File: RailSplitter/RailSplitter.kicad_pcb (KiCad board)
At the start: 2 copper layers, 75 x 45 mm, 24 parts, among them J1 Screw_Terminal_01x02, J2 Screw_Terminal_01x03, Q1 DMP6180SK3, Q2 NJVMJB42CT4G, Q3 NJVMJB41CT4G, U1 OPA990

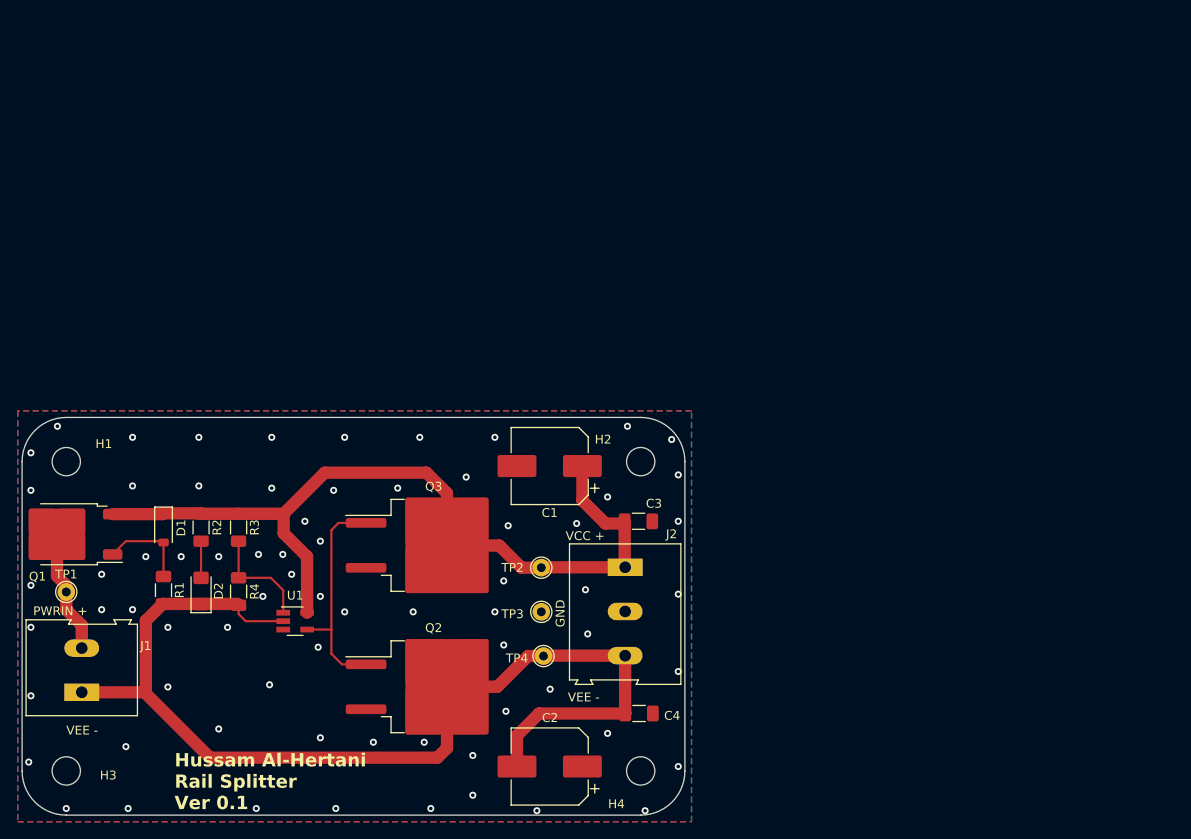
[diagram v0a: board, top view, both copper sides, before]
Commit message: Sat: Apr 27 Added Dual H-Bridge Daughterboard and fixed railsplitter
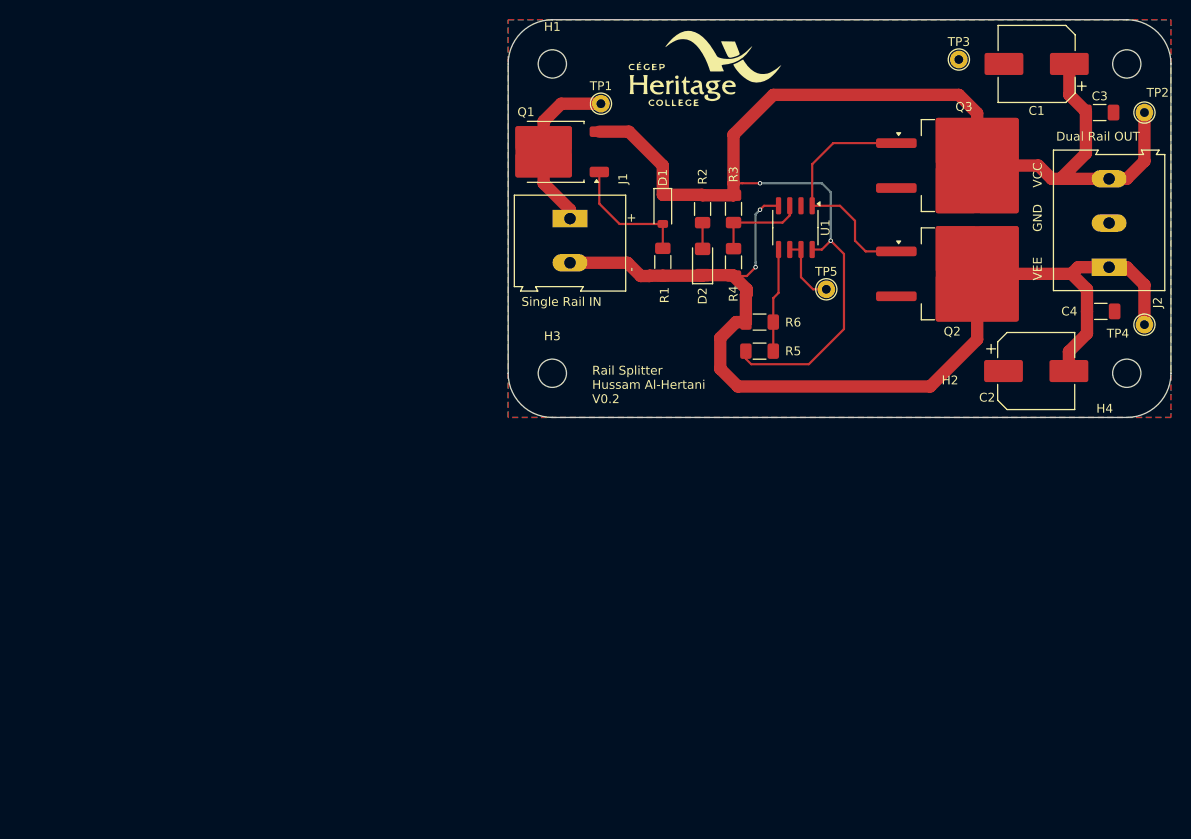
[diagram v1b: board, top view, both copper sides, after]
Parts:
- added G***: LOGO, logos:heritage-logo-small, F.Cu at (172.0, 55.5)
- added R5: 10k, Resistor_SMD:R_1206_3216Metric_Pad1.30x1.75mm_HandSolder, F.Cu at (178.4, 87.5)
- added R6: 10k, Resistor_SMD:R_1206_3216Metric_Pad1.30x1.75mm_HandSolder, F.Cu at (178.4, 84.2)
- added TP5: TestPoint, TestPoint:TestPoint_THTPad_D2.0mm_Drill1.0mm, F.Cu at (186.0, 80.5)
- U1: value OPA990 -> OPA2990IDR; footprint Package_TO_SOT_SMD:SOT-23-5_HandSoldering -> Package_SO:SOIC-8_3.9x4.9mm_P1.27mm
- moved TP2 85.5 mm to (222.0, 60.5)
- moved TP1 81.9 mm to (160.5, 59.5)
- moved TP3 78.4 mm to (201.0, 54.5)
- moved TP4 77.7 mm to (222.0, 84.5)
- moved J1 77.0 mm to (157.0, 72.5), turned to -90 degrees
- moved Q2 76.0 mm to (201.6, 78.8)
- moved Q3 73.8 mm to (201.6, 66.5)
- moved U1 72.0 mm to (182.5, 73.5), turned to -90 degrees
- moved C1 71.5 mm to (209.8, 55.0)
- moved H1 71.1 mm to (155.0, 55.0)
- moved H2 71.1 mm to (220.0, 55.0)
- moved H3 71.1 mm to (155.0, 90.0)
- moved H4 71.1 mm to (220.0, 90.0)
- moved C2 70.9 mm to (209.8, 89.8), turned to 0 degrees
- moved Q1 70.0 mm to (155.3, 64.9)
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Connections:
- J1 pad 1: VEE -> /PWRIN
- J1 pad 2: /PWRIN -> VEE
- J2 pad 1: VCC -> VEE
- J2 pad 3: VEE -> VCC
- R3 pad 2: Net-(U1-+) -> Net-(U1A-+)
- R4 pad 1: Net-(U1-+) -> Net-(U1A-+)
- U1 pad 1: Net-(U1-+) -> Net-(Q2-B)
- U1 pad 2: VEE -> GND
- U1 pad 3: GND -> Net-(U1A-+)
- U1 pad 4: Net-(Q2-B) -> VEE
- U1 pad 5: VCC -> Net-(U1B-+)
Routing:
- net VCC: track 95.2 -> 147.9 mm, vias 0 -> 2
- net Net-(U1-+): track 12.3 -> 0.00 mm
- net Net-(U1B-+): track 0.00 -> 11.7 mm
- net Net-(U1A-+): track 0.00 -> 10.7 mm
- net Net-(U1B--): track 0.00 -> 7.84 mm
- net /PWRIN: track 14.0 -> 19.6 mm
- net Net-(D1-A): track 10.3 -> 14.5 mm
- net Net-(Q2-B): track 25.4 -> 28.2 mm
- net VEE: track 122.6 -> 120.8 mm, vias 0 -> 2
- net Net-(D2-A): track 4.15 -> 2.96 mm
- net GND: vias 71 -> 0
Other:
- board text added: "+"
- board text added: "-"
- board text added: "Dual Rail OUT"
- board text added: "Rail Splitter Hussam Al-Hertani V0.2"
- board text added: "Single Rail IN"
- board text added: "VCC"
- board text added: "VEE"
- board text removed: "Hussam Al-Hertani Rail Splitter Ver 0.1"
- board text removed: "PWRIN +"
- board text removed: "VCC +"
- board text removed: "VEE -"

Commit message: Added16 Channel Servo controller Design
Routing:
- net GND: vias 0 -> 90

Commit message: created _latest gerber sets and added digikey boms. Also did some project cleanup WedMay82024
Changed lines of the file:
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@@
 			(size 1.425 1.75)
 			(layers "F.Cu" "F.Paste" "F.Mask")
-			(roundrect_rratio 0.175439)
+			(roundrect_rratio 0.1754392982)
 			(net 3 "VEE")
 			(pinfunction "K")
@@
 			(size 1.425 1.75)
 			(layers "F.Cu" "F.Paste" "F.Mask")
-			(roundrect_rratio 0.175439)
+			(roundrect_rratio 0.1754392982)
 			(net 5 "Net-(D2-A)")
 			(pinfunction "A")
@@
 			(size 4.6 1.1)
 			(layers "F.Cu" "F.Paste" "F.Mask")
-			(roundrect_rratio 0.227273)
+			(roundrect_rratio 0.2272727273)
 			(net 7 "Net-(Q2-B)")
 			(pinfunction "B")
@@
 			(size 4.55 5.25)
 			(layers "F.Cu" "F.Paste")
-			(roundrect_rratio 0.054945)
+			(roundrect_rratio 0.05494505495)
 			(net 1 "VCC")
 			(pinfunction "C")
@@
 			(size 4.55 5.25)
 			(layers "F.Cu" "F.Paste")
-			(roundrect_rratio 0.054945)
+			(roundrect_rratio 0.05494505495)
 			(net 1 "VCC")
 			(pinfunction "C")
@@
 			(size 9.4 10.8)
 			(layers "F.Cu" "F.Mask")
-			(roundrect_rratio 0.026596)
+			(roundrect_rratio 0.02659595745)
 			(net 1 "VCC")
 			(pinfunction "C")
@@
 			(size 4.55 5.25)
 			(layers "F.Cu" "F.Paste")
-			(roundrect_rratio 0.054945)
+			(roundrect_rratio 0.05494505495)
 			(net 1 "VCC")
 			(pinfunction "C")
@@
 			(size 4.55 5.25)
 			(layers "F.Cu" "F.Paste")
-			(roundrect_rratio 0.054945)
+			(roundrect_rratio 0.05494505495)
 			(net 1 "VCC")
 			(pinfunction "C")
@@
 			(size 4.6 1.1)
 			(layers "F.Cu" "F.Paste" "F.Mask")
-			(roundrect_rratio 0.227273)
+			(roundrect_rratio 0.2272727273)
 			(net 2 "GND")
 			(pinfunction "E")
@@
 			(size 1.3 1.75)
 			(layers "F.Cu" "F.Paste" "F.Mask")
-			(roundrect_rratio 0.192308)
+			(roundrect_rratio 0.1923076923)
 			(net 1 "VCC")
 			(pintype "passive")
@@
 			(size 1.3 1.75)
 			(layers "F.Cu" "F.Paste" "F.Mask")
-			(roundrect_rratio 0.192308)
+			(roundrect_rratio 0.1923076923)
 			(net 5 "Net-(D2-A)")
 			(pintype "passive")
@@
 			(size 1.3 1.75)
 			(layers "F.Cu" "F.Paste" "F.Mask")
-			(roundrect_rratio 0.192308)
+			(roundrect_rratio 0.1923076923)
 			(net 4 "Net-(D1-A)")
 			(pintype "passive")
@@
 			(size 1.3 1.75)
 			(layers "F.Cu" "F.Paste" "F.Mask")
-			(roundrect_rratio 0.192308)
+			(roundrect_rratio 0.1923076923)
 			(net 3 "VEE")
 			(pintype "passive")
@@
 			(size 1.3 1.75)
 			(layers "F.Cu" "F.Paste" "F.Mask")
-			(roundrect_rratio 0.192308)
+			(roundrect_rratio 0.1923076923)
 			(net 1 "VCC")
 			(pintype "passive")
@@
 			(size 1.3 1.75)
 			(layers "F.Cu" "F.Paste" "F.Mask")
-			(roundrect_rratio 0.192308)
+			(roundrect_rratio 0.1923076923)
 			(net 9 "Net-(U1B-+)")
 			(pintype "passive")
@@
 			(size 4.6 1.1)
 			(layers "F.Cu" "F.Paste" "F.Mask")
-			(roundrect_rratio 0.227273)
+			(roundrect_rratio 0.2272727273)
 			(net 7 "Net-(Q2-B)")
 			(pinfunction "B")
@@
 			(size 4.55 5.25)
 			(layers "F.Cu" "F.Paste")
-			(roundrect_rratio 0.054945)
+			(roundrect_rratio 0.05494505495)
 			(net 3 "VEE")
 			(pinfunction "C")
@@
 			(size 4.55 5.25)
 			(layers "F.Cu" "F.Paste")
-			(roundrect_rratio 0.054945)
+			(roundrect_rratio 0.05494505495)
 			(net 3 "VEE")
 			(pinfunction "C")
@@
 			(size 9.4 10.8)
 			(layers "F.Cu" "F.Mask")
-			(roundrect_rratio 0.026596)
+			(roundrect_rratio 0.02659595745)
 			(net 3 "VEE")
 			(pinfunction "C")
@@
 			(size 4.55 5.25)
 			(layers "F.Cu" "F.Paste")
-			(roundrect_rratio 0.054945)
+			(roundrect_rratio 0.05494505495)
 			(net 3 "VEE")
 			(pinfunction "C")
@@
 			(size 4.55 5.25)
 			(layers "F.Cu" "F.Paste")
-			(roundrect_rratio 0.054945)
+			(roundrect_rratio 0.05494505495)
 			(net 3 "VEE")
 			(pinfunction "C")
@@
 			(size 4.6 1.1)
 			(layers "F.Cu" "F.Paste" "F.Mask")
-			(roundrect_rratio 0.227273)
+			(roundrect_rratio 0.2272727273)
 			(net 2 "GND")
 			(pinfunction "E")
@@
 			(size 2.2 1.2)
 			(layers "F.Cu" "F.Paste" "F.Mask")
-			(roundrect_rratio 0.208333)
+			(roundrect_rratio 0.2083333333)
 			(net 4 "Net-(D1-A)")
 			(pinfunction "G")
@@
 			(size 3.05 2.75)
 			(layers "F.Cu" "F.Paste")
-			(roundrect_rratio 0.090909)
+			(roundrect_rratio 0.09090909091)
 			(net 6 "/PWRIN")
 			(pinfunction "D")
@@
 			(size 3.05 2.75)
 			(layers "F.Cu" "F.Paste")
-			(roundrect_rratio 0.090909)
+			(roundrect_rratio 0.09090909091)
 			(net 6 "/PWRIN")
 			(pinfunction "D")
@@
 			(size 6.4 5.8)
 			(layers "F.Cu" "F.Mask")
-			(roundrect_rratio 0.043103)
+			(roundrect_rratio 0.04310293103)
 			(net 6 "/PWRIN")
 			(pinfunction "D")
@@
 			(size 3.05 2.75)
 			(layers "F.Cu" "F.Paste")
-			(roundrect_rratio 0.090909)
+			(roundrect_rratio 0.09090909091)
 			(net 6 "/PWRIN")
 			(pinfunction "D")
@@
 			(size 3.05 2.75)
 			(layers "F.Cu" "F.Paste")
-			(roundrect_rratio 0.090909)
+			(roundrect_rratio 0.09090909091)
 			(net 6 "/PWRIN")
 			(pinfunction "D")
@@
 			(size 2.2 1.2)
 			(layers "F.Cu" "F.Paste" "F.Mask")
-			(roundrect_rratio 0.208333)
+			(roundrect_rratio 0.2083333333)
 			(net 1 "VCC")
 			(pinfunction "S")
@@
 			(size 1.3 1.75)
 			(layers "F.Cu" "F.Paste" "F.Mask")
-			(roundrect_rratio 0.192308)
+			(roundrect_rratio 0.1923076923)
 			(net 9 "Net-(U1B-+)")
 			(pintype "passive")
@@
 			(size 1.3 1.75)
 			(layers "F.Cu" "F.Paste" "F.Mask")
-			(roundrect_rratio 0.192308)
+			(roundrect_rratio 0.1923076923)
 			(net 3 "VEE")
 			(pintype "passive")
@@
 			(size 1.325 1.8)
 			(layers "F.Cu" "F.Paste" "F.Mask")
-			(roundrect_rratio 0.188679)
+			(roundrect_rratio 0.1886792453)
 			(net 1 "VCC")
 			(pintype "passive")
@@
 			(size 1.325 1.8)
 			(layers "F.Cu" "F.Paste" "F.Mask")
-			(roundrect_rratio 0.188679)
+			(roundrect_rratio 0.1886792453)
 			(net 2 "GND")
 			(pintype "passive")
@@
 			(size 1.325 1.8)
 			(layers "F.Cu" "F.Paste" "F.Mask")
-			(roundrect_rratio 0.188679)
+			(roundrect_rratio 0.1886792453)
 			(net 2 "GND")
 			(pintype "passive")
@@
 			(size 1.325 1.8)
 			(layers "F.Cu" "F.Paste" "F.Mask")
-			(roundrect_rratio 0.188679)
+			(roundrect_rratio 0.1886792453)
 			(net 3 "VEE")
 			(pintype "passive")
@@
 			(size 1.3 1.75)
 			(layers "F.Cu" "F.Paste" "F.Mask")
-			(roundrect_rratio 0.192308)
+			(roundrect_rratio 0.1923076923)
 			(net 8 "Net-(U1A-+)")
 			(pintype "passive")
@@
 			(size 1.3 1.75)
 			(layers "F.Cu" "F.Paste" "F.Mask")
-			(roundrect_rratio 0.192308)
+			(roundrect_rratio 0.1923076923)
 			(net 3 "VEE")
 			(pintype "passive")
@@
 			(size 1.3 1.75)
 			(layers "F.Cu" "F.Paste" "F.Mask")
-			(roundrect_rratio 0.192308)
+			(roundrect_rratio 0.1923076923)
 			(net 1 "VCC")
 			(pintype "passive")
@@
 			(size 1.3 1.75)
 			(layers "F.Cu" "F.Paste" "F.Mask")
-			(roundrect_rratio 0.192308)
+			(roundrect_rratio 0.1923076923)
 			(net 8 "Net-(U1A-+)")
 			(pintype "passive")
